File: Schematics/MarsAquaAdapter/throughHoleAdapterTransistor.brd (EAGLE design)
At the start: 50.8 x 32.7 mm, 26 parts, among them IC3 LMV358SOIC, J0 0k, J3 0k, Q1 MMBT4403, Q2 MMBT4403

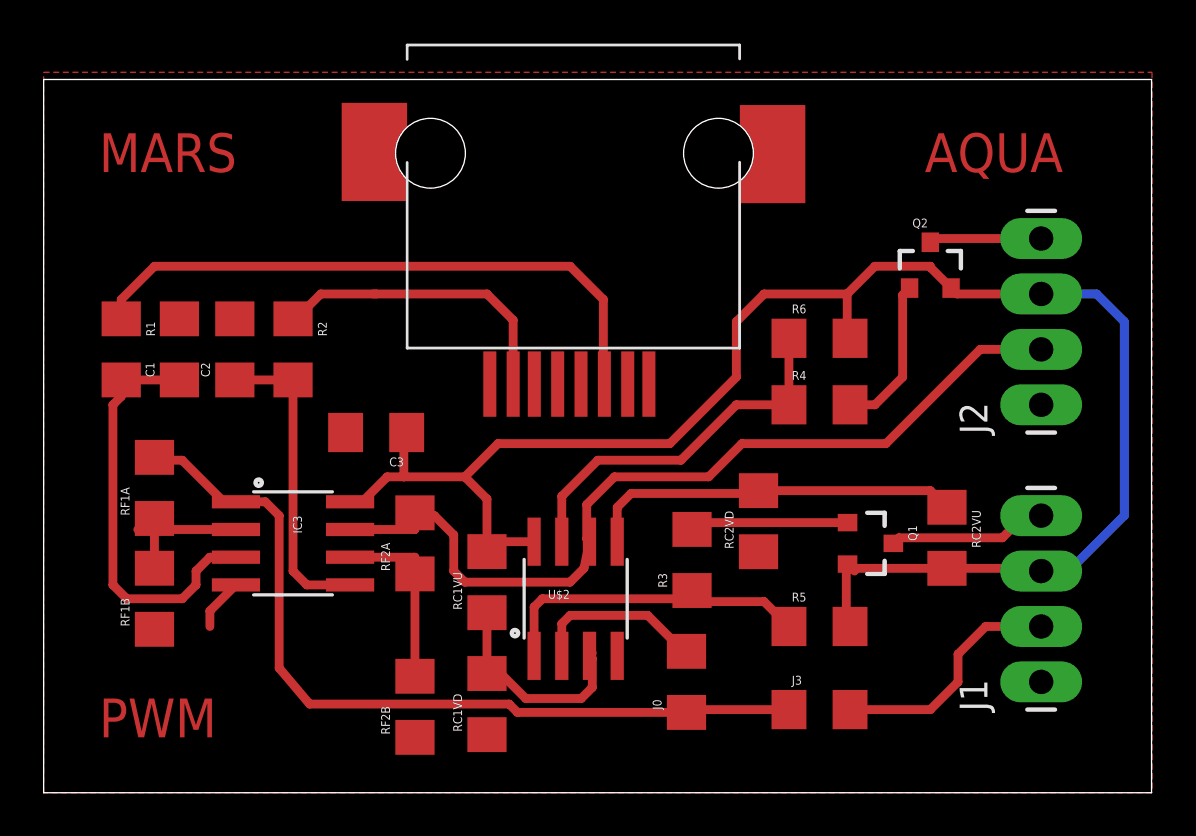
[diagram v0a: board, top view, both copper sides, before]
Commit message: New breakout with PH, temp, and moisture sensor
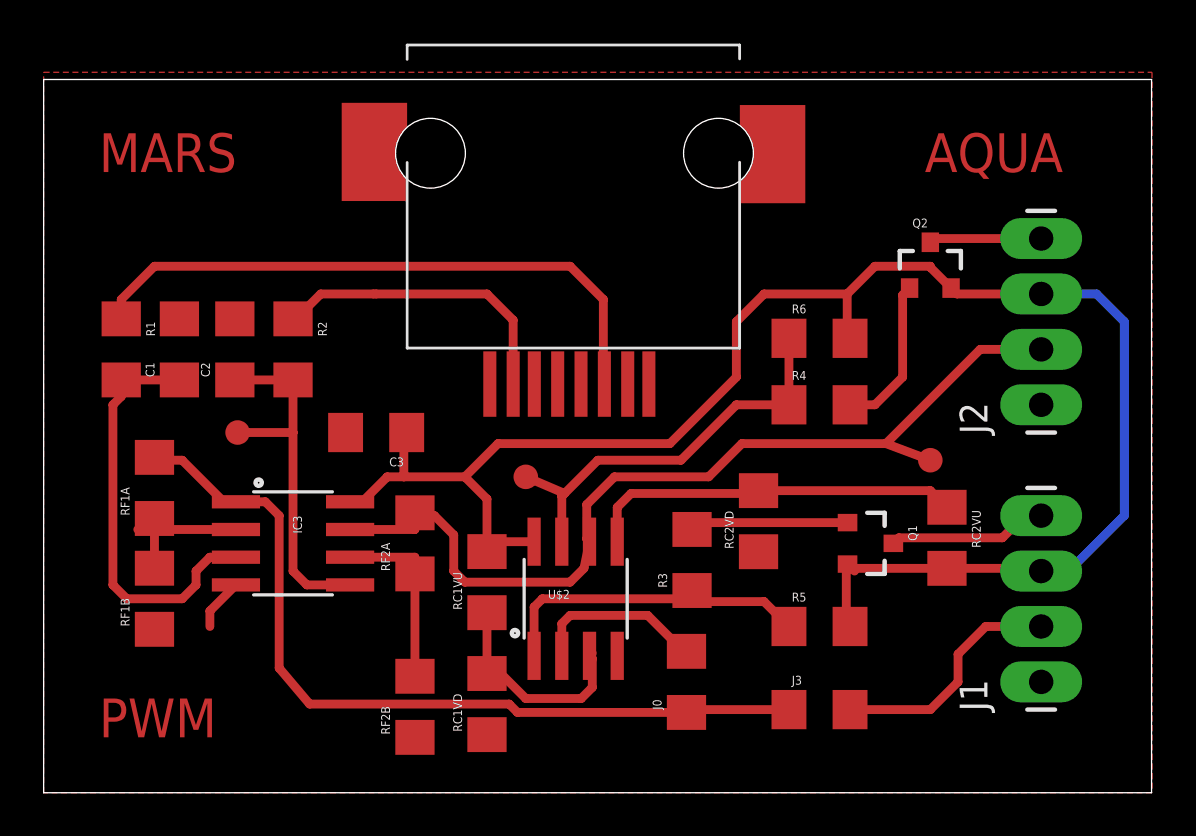
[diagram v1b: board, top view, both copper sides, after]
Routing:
- net N$8: track 14.3 -> 16.9 mm
- net BLUE_OUTPUT: track 40.8 -> 42.9 mm
- net N$11: track 17.3 -> 19.2 mm
